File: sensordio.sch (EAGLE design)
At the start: 16 parts, among them IC1 PCA9534D, IC2 ULN2003AD

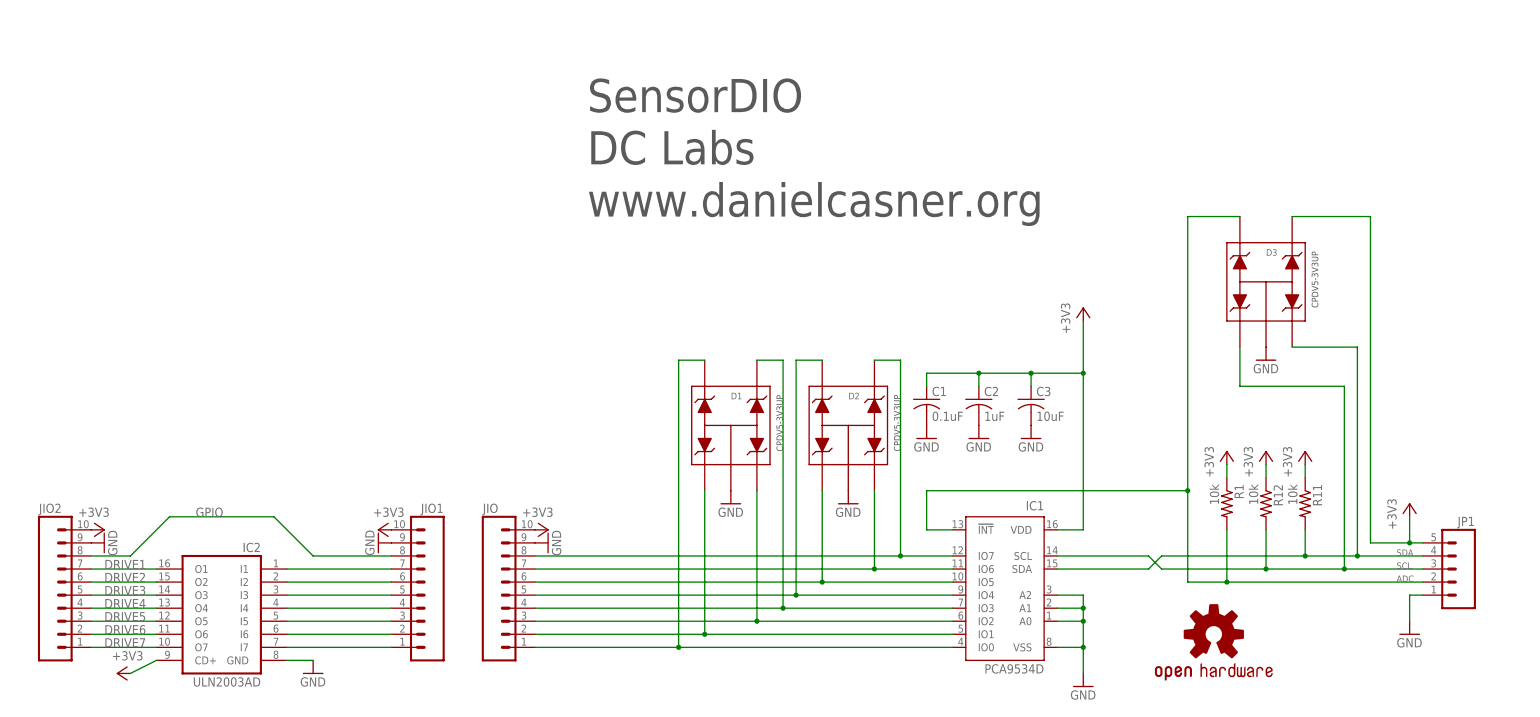
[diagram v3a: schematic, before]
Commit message: Add boxes around components
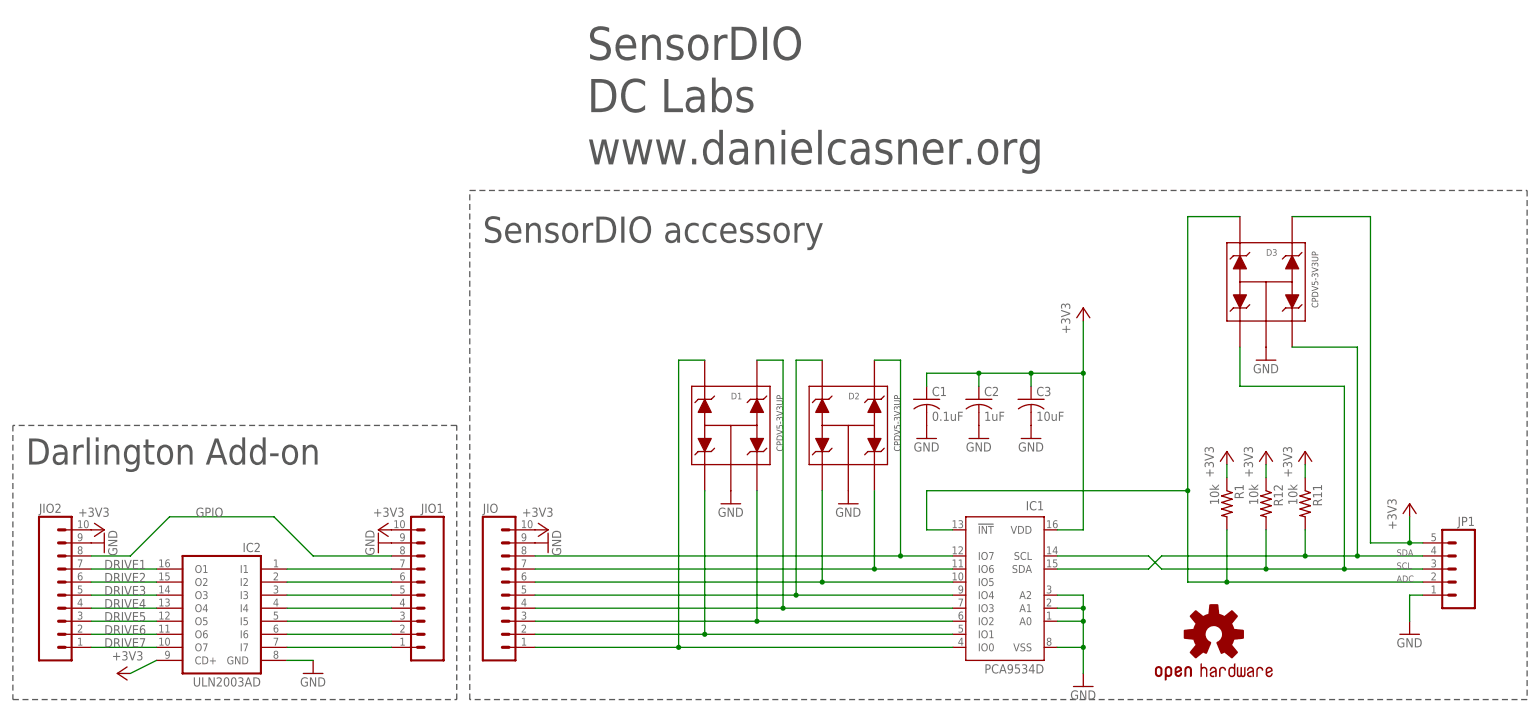
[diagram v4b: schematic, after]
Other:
- note added: "Darlington Add-on"
- note added: "SensorDIO accessory"
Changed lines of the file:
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@@
 <sheet>
 <plain>
-<text x="-78.74" y="96.52" size="6.4516" layer="97">DC Labs</text>
-<text x="-78.74" y="86.36" size="6.4516" layer="97">www.danielcasner.org</text>
-<text x="-78.74" y="106.68" size="6.4516" layer="97">SensorDIO</text>
+<text x="-78.74" y="106.68" size="6.4516" layer="97">DC Labs</text>
+<text x="-78.74" y="96.52" size="6.4516" layer="97">www.danielcasner.org</text>
+<text x="-78.74" y="116.84" size="6.4516" layer="97">SensorDIO</text>
+<wire x1="-101.6" y1="-7.62" x2="-101.6" y2="91.44" width="0.1524" layer="97" style="longdash"/>
+<wire x1="-101.6" y1="91.44" x2="104.14" y2="91.44" width="0.1524" layer="97" style="longdash"/>
+<wire x1="104.14" y1="91.44" x2="104.14" y2="-7.62" width="0.1524" layer="97" style="longdash"/>
+<wire x1="104.14" y1="-7.62" x2="-101.6" y2="-7.62" width="0.1524" layer="97" style="longdash"/>
+<wire x1="-104.14" y1="-7.62" x2="-104.14" y2="45.72" width="0.1524" layer="97" style="longdash"/>
+<wire x1="-104.14" y1="45.72" x2="-190.5" y2="45.72" width="0.1524" layer="97" style="longdash"/>
+<wire x1="-190.5" y1="45.72" x2="-190.5" y2="-7.62" width="0.1524" layer="97" style="longdash"/>
+<wire x1="-190.5" y1="-7.62" x2="-104.14" y2="-7.62" width="0.1524" layer="97" style="longdash"/>
+<text x="-99.06" y="81.28" size="5.08" layer="97">SensorDIO accessory</text>
+<text x="-187.96" y="38.1" size="5.08" layer="97">Darlington Add-on</text>
 </plain>
 <instances>

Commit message: Add very rough beginning of a layout for SensorDIO
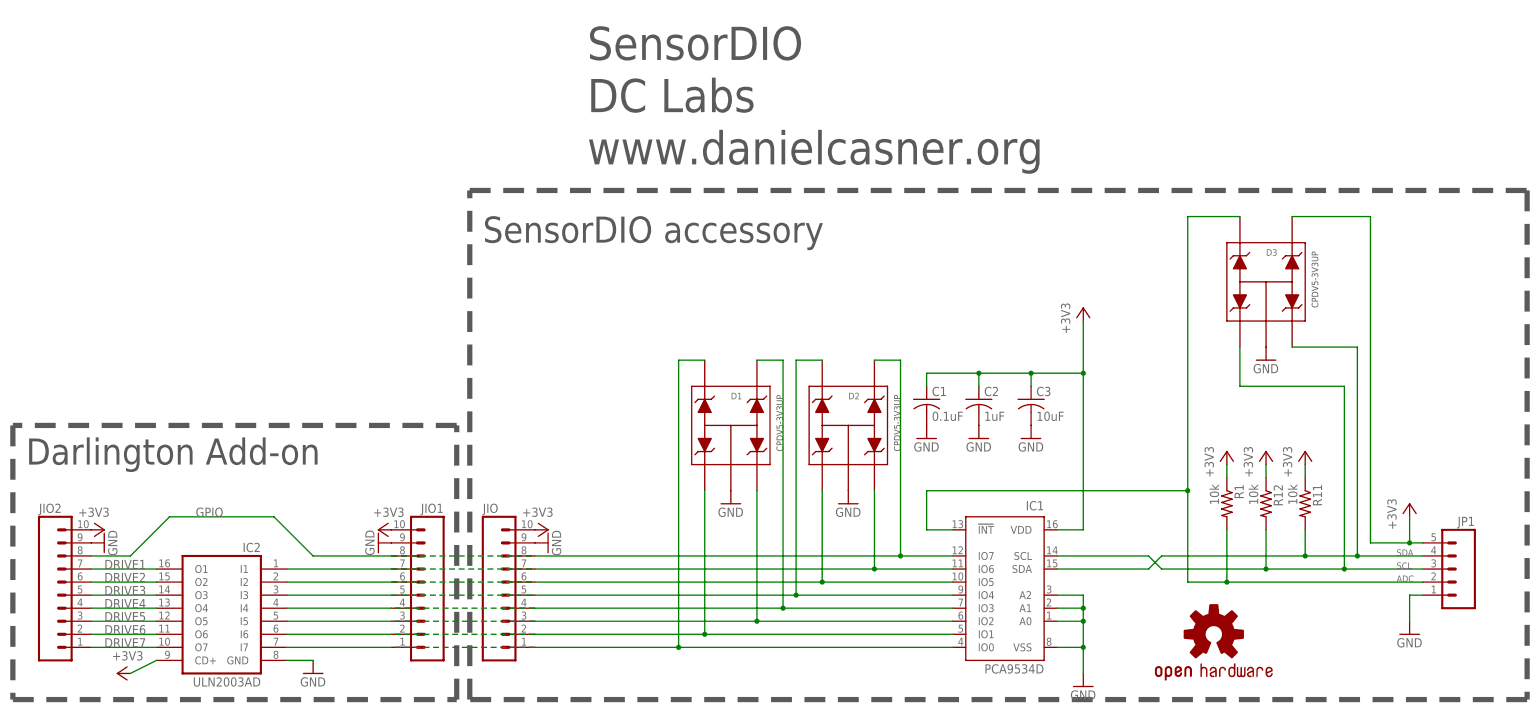
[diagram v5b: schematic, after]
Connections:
- removed net N$10: IC2.I6, JIO1.2
- removed net N$11: IC2.I5, JIO1.3
- removed net N$12: IC2.I4, JIO1.4
- removed net N$13: IC2.I3, JIO1.5
- removed net N$14: IC2.I2, JIO1.6
- removed net N$15: IC2.I1, JIO1.7
- removed net N$2: D1.P$5, IC1.IO0, JIO.1
- removed net N$9: D2.P$4, IC1.IO7, JIO.8
- net GPIO: now also D2.P$4, IC1.IO7, JIO.8
- net N$1: now also D1.P$5, IC1.IO0, JIO.1
- net N$3: now also IC2.I6, JIO1.2
- net N$4: now also IC2.I5, JIO1.3
- net N$5: now also IC2.I4, JIO1.4
- net N$6: now also IC2.I3, JIO1.5
- net N$7: now also IC2.I2, JIO1.6
- net N$8: now also IC2.I1, JIO1.7
